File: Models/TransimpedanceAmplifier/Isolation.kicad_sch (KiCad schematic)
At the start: 0 parts

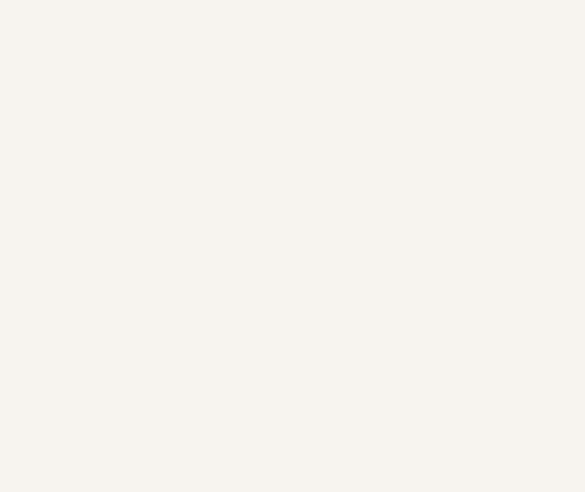
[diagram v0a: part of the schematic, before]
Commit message: Got the digital isolator chip
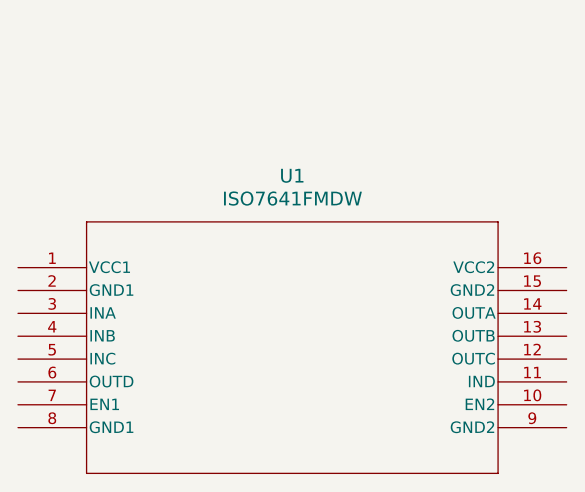
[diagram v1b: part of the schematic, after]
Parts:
- added U1: ISO7641FMDW, DW16, symbol ISO7641FM:ISO7641FMDW
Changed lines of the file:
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@@
+		)
+	)
+	(symbol
+		(lib_id "ISO7641FM:ISO7641FMDW")
+		(at 93.98 81.28 0)
+		(unit 1)
+		(exclude_from_sim no)
+		(in_bom yes)
+		(on_board yes)
+		(dnp no)
+		(fields_autoplaced yes)
+		(property "Reference" "U1"
+			(at 124.46 71.12 0)
+			(effects
+				(font
+					(size 1.524 1.524)
+				)
+			)
+		)
+		(property "Value" "ISO7641FMDW"
+			(at 124.46 73.66 0)
+			(effects
+				(font
+					(size 1.524 1.524)
+				)
+			)
+		)
+		(property "Footprint" "DW16"
+			(at 93.98 81.28 0)
+			(effects
+				(font
+					(size 1.27 1.27)
+					(italic yes)
+				)
+				(hide yes)
+			)
+		)
+		(property "Datasheet" "https://www.ti.com/lit/gpn/iso7641fm"
+			(at 93.98 81.28 0)
+			(effects
+				(font
+					(size 1.27 1.27)
+					(italic yes)
+				)
+				(hide yes)
+			)
+		)
+		(property "Description" ""
+			(at 93.98 81.28 0)
+			(effects
+				(font
+					(size 1.27 1.27)
+				)
+				(hide yes)
+			)
+		)
+		(property "Purchase Link" "https://www.digikey.com/en/products/detail/texas-instruments/ISO7641FMDWR/2799299"
+			(at 93.98 81.28 0)
+			(effects
+				(font
+					(size 1.27 1.27)
+				)
+				(hide yes)
+			)
+		)
+		(pin "1"
+		)
+		(pin "2"
+		)
+		(pin "3"
+		)
+		(pin "4"
+		)
+		(pin "5"
+		)
+		(pin "6"
+		)
+		(pin "7"
+		)
+		(pin "10"
+		)
+		(pin "9"
+		)
+		(pin "14"
+		)
+		(pin "13"
+		)
+		(pin "12"
+		)
+		(pin "11"
+		)
+		(pin "8"
+		)
+		(pin "16"
+		)
+		(pin "15"
+		)
+		(instances
+			(project ""
+				(path "/ec9f2ae3-e40d-40eb-9760-2b611ee8efd1/7e303428-a18c-4ad4-b002-5ab9c6631588/e0dacc02-a437-4540-b76e-19ca4ea6e74c"
+					(reference "U1")
+					(unit 1)
+				)
+			)
 		)
 	)

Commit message: Save progress
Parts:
- added C11, C12, C13, C14: 100 nF, symbol Device:C
- added U14: ISO7641FMDW, DW16, symbol ISO7641FM:ISO7641FMDW
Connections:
- net 3.3V_Digital: now reaches U1.1 (VCC1)
- net 3.3V_Digital: now also U1.7 (EN1), C13.2, C14.2, U14.1 (VCC1), U14.7 (EN1)
- net 3.3V_Analog: now reaches U1.10 (EN2)
- net 3.3V_Analog: now also U1.16 (VCC2), C11.2, C12.2, U14.10 (EN2), U14.16 (VCC2)
- net MISO_DAC_Analog: now reaches U1.11 (IND)
- net MOSI_DAC_Analog: now reaches U1.12 (OUTC)
- net SCK_DAC_Analog: now reaches U1.13 (OUTB)
- net CS_DAC_Analog: now reaches U1.14 (OUTA)
- net GND_Analog: now reaches U1.15 (GND2)
- net GND_Analog: now also U1.9 (GND2), C11.1, C12.1, U14.15 (GND2), U14.9 (GND2)
- net GND_Digital: now reaches U1.2 (GND1)
- net GND_Digital: now also U1.8 (GND1), C13.1, C14.1, U14.2 (GND1), U14.8 (GND1)
- net CS_DAC_Digital: now reaches U1.3 (INA)
- net SCK_Digital: now reaches U1.4 (INB)
- net SCK_Digital: now also U14.4 (INB)
- net MOSI_Digital: now reaches U1.5 (INC)
- net MOSI_Digital: now also U14.5 (INC)
- net MISO_Digital: now reaches U1.6 (OUTD)
- net MISO_Digital: now also U14.6 (OUTD)
- new net CS_ADC_Analog: U14.14 (OUTA)
- new net CS_ADC_Digital: U14.3 (INA)
- new net MISO_ADC_Analog: U14.11 (IND)
- new net MOSI_ADC_Analog: U14.12 (OUTC)
- new net SCK_ADC_Analog: U14.13 (OUTB)
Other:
- note added: "Analog"
- note added: "Current demands for ISO7641FM @ 3.3 V 0 Mbps rate condition: I_CC1 = 2.0 mA I_CC2 = 3.6 mA 25 Mbps rate condition: I_CC1 = 3.6 mA I_CC2 = 6.0 mA 50 Mbps rate condition: I_CC1 = 4.8 mA I_CC2 = 8.8 mA"
- note added: "Digital"
- note added: "Specifications from table instead of graph: 0 Mbps rate condition: I_CC1 = 2.0-3.0 mA I_CC2 = 3.3-5.0 mA 25 Mbps rate condition: I_CC1 = 3.4-4.5 mA I_CC2 = 6.1-7.6 mA 50 Mbps rate condition (extrapolation): I_CC1 = 4.8-6.1 mA I_CC2 = 8.8-10.8 mA"
- note added: "TODO: Reorder SPI pins based on which arrangement best suits the physical layout of the receiving chip's pins"
- note removed: "Specific chips and power requirements for the isolators are not specified yet. Current demands are likely 5-10 mA per SPI port."
- moved on the sheet: U1

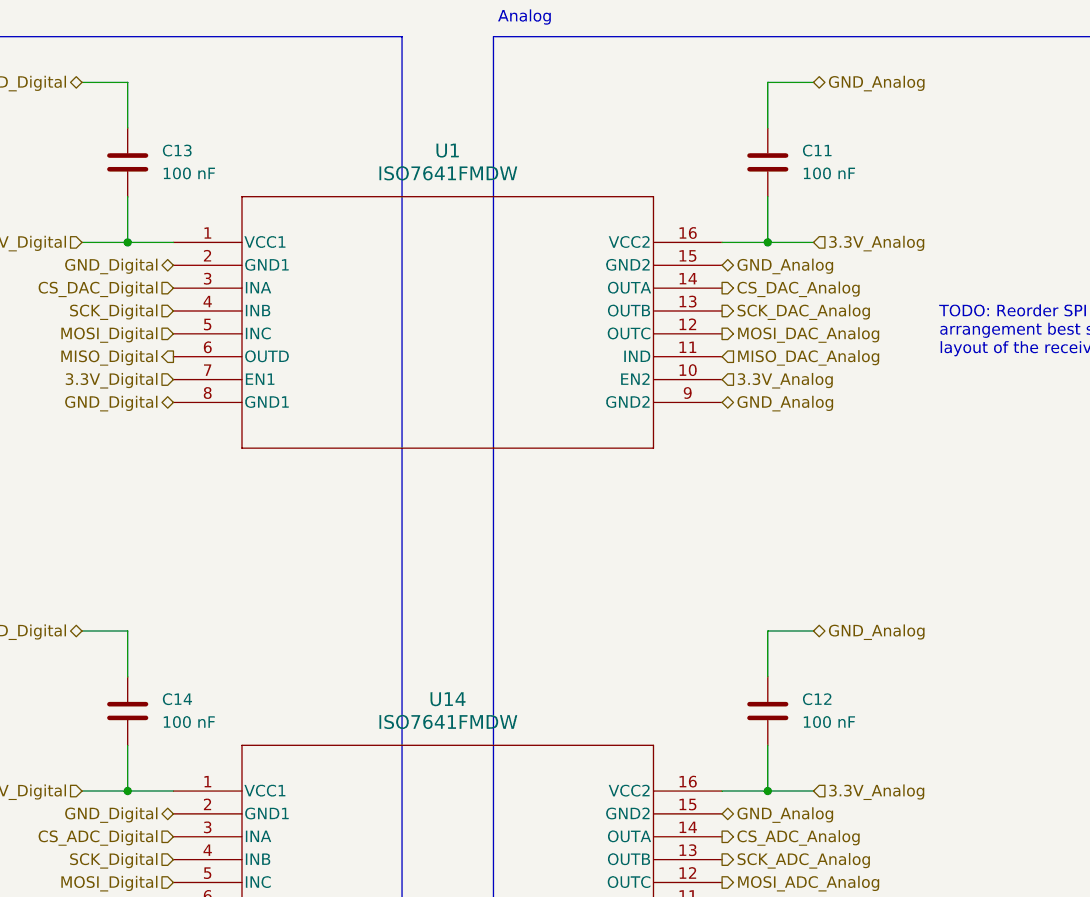
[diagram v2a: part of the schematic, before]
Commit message: Added purchase links for all current capacitors, with dimensional tolerances matching the footprint
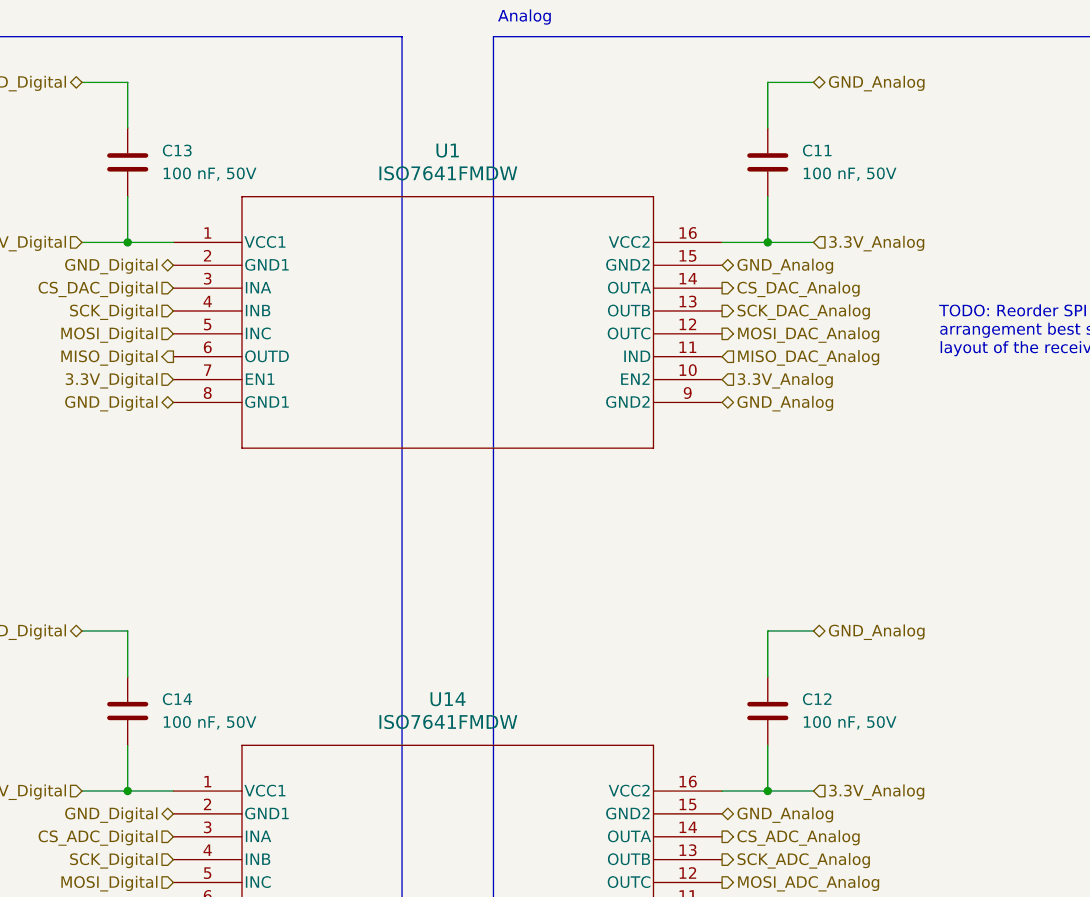
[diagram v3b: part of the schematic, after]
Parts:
- C11, C12, C13, C14: value 100 nF -> 100 nF, 50V; Purchase Link (none) -> https://www.digikey.com/en/products/detail/murata-electroni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
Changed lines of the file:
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@@
 			)
 		)
-		(property "Value" "100 nF"
+		(property "Value" "100 nF, 50V"
 			(at 120.65 99.0599 0)
 			(effects
@@
 		)
 		(property "Description" "Unpolarized capacitor"
+			(at 116.84 97.79 0)
+			(effects
+				(font
+					(size 1.27 1.27)
+				)
+				(hide yes)
+			)
+		)
+		(property "Purchase Link" "https://www.digikey.com/en/products/detail/murata-electronics/GCM188L81H104KA57J/17846871"
 			(at 116.84 97.79 0)
 			(effects
@@
 			)
 		)
-		(property "Value" "100 nF"
+		(property "Value" "100 nF, 50V"
 			(at 191.77 38.0999 0)
 			(effects
@@
 		)
 		(property "Description" "Unpolarized capacitor"
+			(at 187.96 36.83 0)
+			(effects
+				(font
+					(size 1.27 1.27)
+				)
+				(hide yes)
+			)
+		)
+		(property "Purchase Link" "https://www.digikey.com/en/products/detail/murata-electronics/GCM188L81H104KA57J/17846871"
 			(at 187.96 36.83 0)
 			(effects
@@
 			)
 		)
-		(property "Value" "100 nF"
+		(property "Value" "100 nF, 50V"
 			(at 191.77 99.0599 0)
 			(effects
@@
 		)
 		(property "Description" "Unpolarized capacitor"
+			(at 187.96 97.79 0)
+			(effects
+				(font
+					(size 1.27 1.27)
+				)
+				(hide yes)
+			)
+		)
+		(property "Purchase Link" "https://www.digikey.com/en/products/detail/murata-electronics/GCM188L81H104KA57J/17846871"
 			(at 187.96 97.79 0)
 			(effects
@@
 			)
 		)
-		(property "Value" "100 nF"
+		(property "Value" "100 nF, 50V"
 			(at 120.65 38.0999 0)
 			(effects
@@
 			(at 116.84 36.83 0)
 			(effects
+				(font
+					(size 1.27 1.27)
+				)
+				(hide yes)
+			)
+		)
+		(property "Purchase Link" "https://www.digikey.com/en/products/detail/murata-electronics/GCM188L81H104KA57J/17846871"
+			(at 116.84 36.83 0)
+			(effects

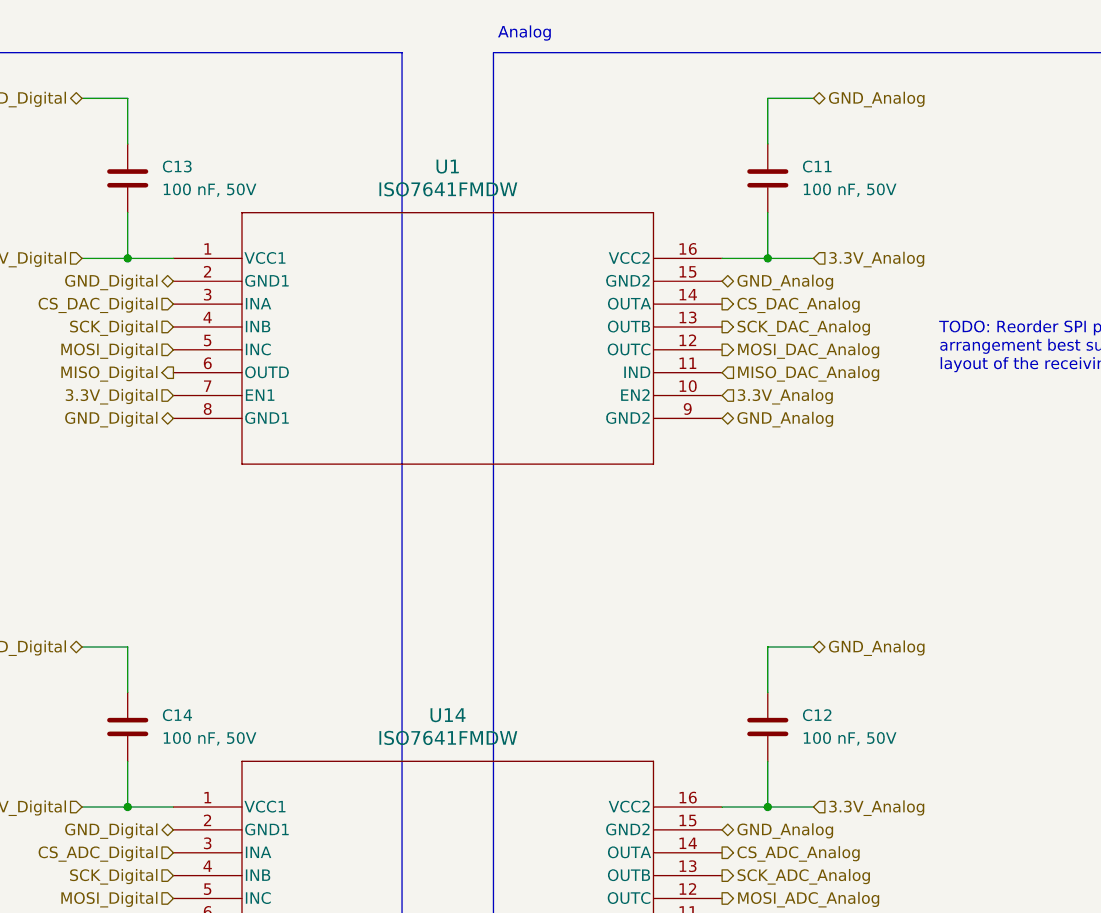
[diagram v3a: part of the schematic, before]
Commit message: Finished writing the ADC's network
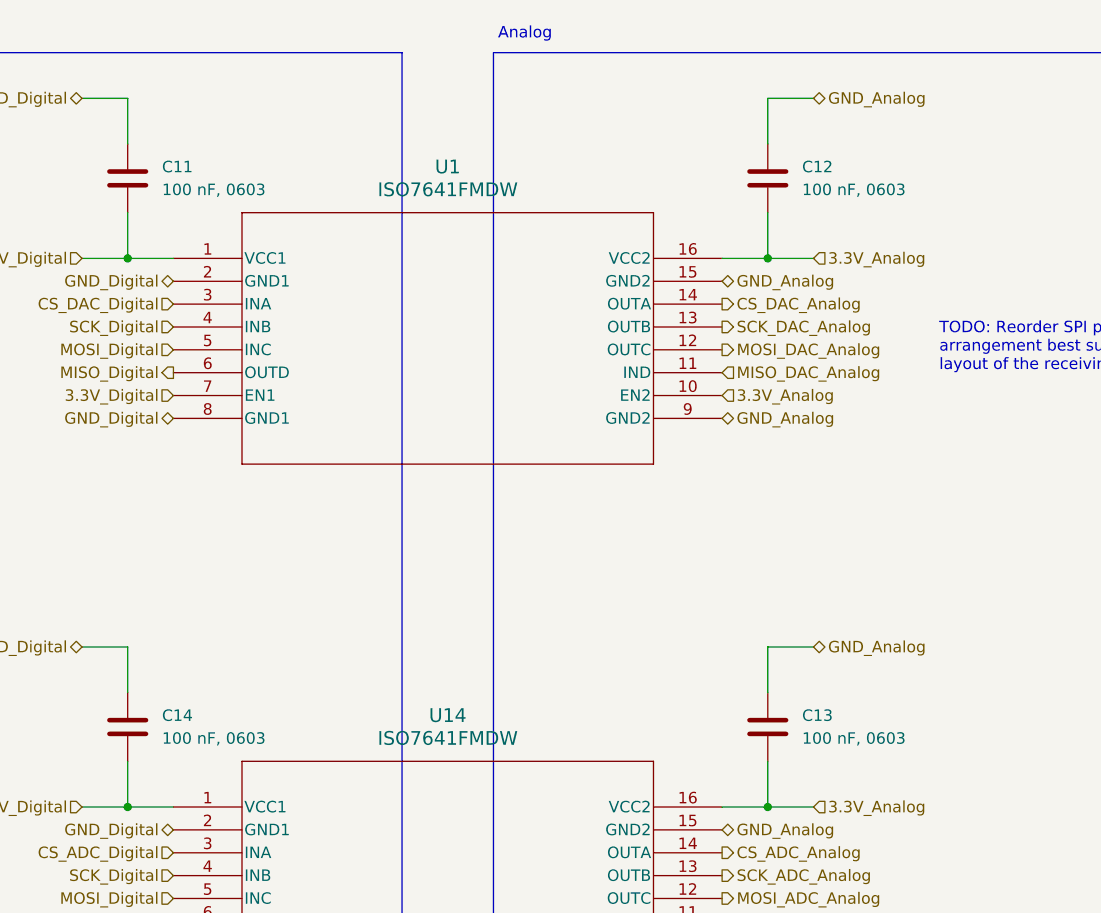
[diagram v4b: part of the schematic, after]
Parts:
- C11, C12, C13, C14: value 100 nF, 50V -> 100 nF, 0603; Purchase Link https://www.digikey.com/en/products/detail/murata-electroni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 -> (none)
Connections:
- net 3.3V_Analog: now also C13.2; no longer C11.2
- net 3.3V_Digital: now also C11.2; no longer C13.2
- net GND_Analog: now also C13.1; no longer C11.1
- net GND_Digital: now also C11.1; no longer C13.1
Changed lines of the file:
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@@
 			)
 		)
-		(property "Value" "100 nF, 50V"
+		(property "Value" "100 nF, 0603"
 			(at 120.65 99.0599 0)
 			(effects
@@
 			)
 		)
-		(property "Purchase Link" "https://www.digikey.com/en/products/detail/murata-electronics/GCM188L81H104KA57J/17846871"
-			(at 116.84 97.79 0)
-			(effects
-				(font
-					(size 1.27 1.27)
-				)
-				(hide yes)
-			)
-		)
-		(pin "1"
-		)
-		(pin "2"
+		(pin "2"
+		)
+		(pin "1"
 		)
 		(instances
@@
 	(symbol
 		(lib_id "Device:C")
-		(at 187.96 36.83 0)
+		(at 116.84 36.83 0)
 		(unit 1)
 		(exclude_from_sim no)
@@
 		(fields_autoplaced yes)
 		(property "Reference" "C11"
-			(at 191.77 35.5599 0)
-			(effects
-				(font
-					(size 1.27 1.27)
-				)
-				(justify left)
-			)
-		)
-		(property "Value" "100 nF, 50V"
-			(at 191.77 38.0999 0)
+			(at 120.65 35.5599 0)
+			(effects
+				(font
+					(size 1.27 1.27)
+				)
+				(justify left)
+			)
+		)
+		(property "Value" "100 nF, 0603"
+			(at 120.65 38.0999 0)
 			(effects
 				(font
@@
 		)
 		(property "Footprint" ""
-			(at 188.9252 40.64 0)
+			(at 117.8052 40.64 0)
 			(effects
 				(font
@@
 		)
 		(property "Datasheet" "~"
-			(at 187.96 36.83 0)
+			(at 116.84 36.83 0)
 			(effects
 				(font
@@
 		)
 		(property "Description" "Unpolarized capacitor"
-			(at 187.96 36.83 0)
-			(effects
-				(font
-					(size 1.27 1.27)
-				)
-				(hide yes)
-			)
-		)
-		(property "Purchase Link" "https://www.digikey.com/en/products/detail/murata-electronics/GCM188L81H104KA57J/17846871"
-			(at 187.96 36.83 0)
-			(effects
-				(font
-					(size 1.27 1.27)
-				)
-				(hide yes)
-			)
-		)
-		(pin "1"
-		)
-		(pin "2"
+			(at 116.84 36.83 0)
+			(effects
+				(font
+					(size 1.27 1.27)
+				)
+				(hide yes)
+			)
+		)
+		(pin "2"
+		)
+		(pin "1"
 		)
 		(instances
@@
 	(symbol
 		(lib_id "Device:C")
+		(at 187.96 36.83 0)
+		(unit 1)
+		(exclude_from_sim no)
+		(in_bom yes)
+		(on_board yes)
+		(dnp no)
+		(fields_autoplaced yes)
+		(property "Reference" "C12"
+			(at 191.77 35.5599 0)
+			(effects
+				(font
+					(size 1.27 1.27)
+				)
+				(justify left)
+			)
+		)
+		(property "Value" "100 nF, 0603"
+			(at 191.77 38.0999 0)
+			(effects
+				(font
+					(size 1.27 1.27)
+				)
+				(justify left)
+			)
+		)
+		(property "Footprint" ""
+			(at 188.9252 40.64 0)
+			(effects
+				(font
+					(size 1.27 1.27)
+				)
+				(hide yes)
+			)
+		)
+		(property "Datasheet" "~"
+			(at 187.96 36.83 0)
+			(effects
+				(font
+					(size 1.27 1.27)
+				)
+				(hide yes)
+			)
+		)
+		(property "Description" "Unpolarized capacitor"
+			(at 187.96 36.83 0)
+			(effects
+				(font
+					(size 1.27 1.27)
+				)
+				(hide yes)
+			)
+		)
+		(pin "2"
+		)
+		(pin "1"
+		)
+		(instances
+			(project "TransimpedanceAmplifier"
+				(path "/ec9f2ae3-e40d-40eb-9760-2b611ee8efd1/7e303428-a18c-4ad4-b002-5ab9c6631588/e0dacc02-a437-4540-b76e-19ca4ea6e74c"
+					(reference "C12")
+					(unit 1)
+				)
+			)
+		)
+	)
+	(symbol
+		(lib_id "Device:C")
 		(at 187.96 97.79 0)
 		(unit 1)
@@
 		(dnp no)
 		(fields_autoplaced yes)
-		(property "Reference" "C12"
+		(property "Reference" "C13"
 			(at 191.77 96.5199 0)
 			(effects
@@
 			)
 		)
-		(property "Value" "100 nF, 50V"
+		(property "Value" "100 nF, 0603"
 			(at 191.77 99.0599 0)
 			(effects
@@
 			)
 		)
-		(property "Purchase Link" "https://www.digikey.com/en/products/detail/murata-electronics/GCM188L81H104KA57J/17846871"
-			(at 187.96 97.79 0)
-			(effects
-				(font
-					(size 1.27 1.27)
-				)
-				(hide yes)
-			)
-		)
-		(pin "2"
-		)
-		(pin "1"
-		)
-		(instances
-			(project ""
-				(path "/ec9f2ae3-e40d-40eb-9760-2b611ee8efd1/7e303428-a18c-4ad4-b002-5ab9c6631588/e0dacc02-a437-4540-b76e-19ca4ea6e74c"
-					(reference "C12")
-					(unit 1)
-				)
-			)
-		)
-	)
-	(symbol
-		(lib_id "Device:C")
-		(at 116.84 36.83 0)
-		(unit 1)
-		(exclude_from_sim no)
-		(in_bom yes)
-		(on_board yes)
-		(dnp no)
-		(fields_autoplaced yes)
-		(property "Reference" "C13"
-			(at 120.65 35.5599 0)
-			(effects
-				(font
-					(size 1.27 1.27)
-				)
-				(justify left)
-			)
-		)
-		(property "Value" "100 nF, 50V"
-			(at 120.65 38.0999 0)
-			(effects
-				(font
-					(size 1.27 1.27)
-				)
-				(justify left)
-			)
-		)
-		(property "Footprint" ""
-			(at 117.8052 40.64 0)
-			(effects
-				(font
-					(size 1.27 1.27)
-				)
-				(hide yes)
-			)
-		)
-		(property "Datasheet" "~"
-			(at 116.84 36.83 0)
-			(effects
-				(font
-					(size 1.27 1.27)
-				)
-				(hide yes)
-			)
-		)
-		(property "Description" "Unpolarized capacitor"
-			(at 116.84 36.83 0)
-			(effects
-				(font
-					(size 1.27 1.27)
-				)
-				(hide yes)
-			)
-		)
-		(property "Purchase Link" "https://www.digikey.com/en/products/detail/murata-electronics/GCM188L81H104KA57J/17846871"
-			(at 116.84 36.83 0)
-			(effects
-				(font
-					(size 1.27 1.27)
-				)
-				(hide yes)
-			)
-		)
-		(pin "1"
-		)
-		(pin "2"
-		)
-		(instances
+		(pin "2"
+		)
+		(pin "1"
+		)
+		(instances

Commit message: Finished for today
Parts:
- C11, C12, C13, C14: Purchase Link (none) -> https://www.digikey.com/en/products/detail/murata-electroni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
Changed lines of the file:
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@@
+			)
+		)
+		(property "Purchase Link" "https://www.digikey.com/en/products/detail/murata-electronics/GRM188R72A104KA35D/702549"
+			(at 116.84 97.79 0)
+			(effects
+				(font
+					(size 1.27 1.27)
+				)
+				(hide yes)
 			)
 		)
@@
 			)
 		)
+		(property "Purchase Link" "https://www.digikey.com/en/products/detail/murata-electronics/GRM188R72A104KA35D/702549"
+			(at 116.84 36.83 0)
+			(effects
+				(font
+					(size 1.27 1.27)
+				)
+				(hide yes)
+			)
+		)
 		(pin "2"
 		)
@@
 			)
 		)
+		(property "Purchase Link" "https://www.digikey.com/en/products/detail/murata-electronics/GRM188R72A104KA35D/702549"
+			(at 187.96 36.83 0)
+			(effects
+				(font
+					(size 1.27 1.27)
+				)
+				(hide yes)
+			)
+		)
 		(pin "2"
 		)
@@
 			(at 187.96 97.79 0)
 			(effects
+				(font
+					(size 1.27 1.27)
+				)
+				(hide yes)
+			)
+		)
+		(property "Purchase Link" "https://www.digikey.com/en/products/detail/murata-electronics/GRM188R72A104KA35D/702549"
+			(at 187.96 97.79 0)
+			(effects

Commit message: Save progress
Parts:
- U1, U14: footprint DW16 -> (none)
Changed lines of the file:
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@@
 			)
 		)
-		(property "Footprint" "DW16"
+		(property "Footprint" ""
 			(at 121.92 106.68 0)
 			(effects
@@
 			)
 		)
-		(property "Footprint" "DW16"
+		(property "Footprint" ""
 			(at 121.92 45.72 0)
 			(effects

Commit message: Save progress
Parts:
- removed C11, C12, C13, C14: 100 nF, 0603, symbol Device:C
- ADC_Isolator: renamed from U14; value ISO7641FMDW -> ISO7641FM
- DAC_Isolator: renamed from U1; value ISO7641FMDW -> ISO7641FM
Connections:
- removed net 3.3V_Analog: ADC_Isolator.10 (EN2), ADC_Isolator.16 (VCC2), DAC_Isolator.10 (EN2), DAC_Isolator.16 (VCC2)
- removed net 3.3V_Digital: ADC_Isolator.1 (VCC1), ADC_Isolator.7 (EN1), DAC_Isolator.1 (VCC1), DAC_Isolator.7 (EN1)
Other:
- note added: "Analog / High Voltage"
- note removed: "Analog"
